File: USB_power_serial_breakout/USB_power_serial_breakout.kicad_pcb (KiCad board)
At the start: 2 copper layers, 45.7 x 26.7 mm, 18 parts, among them J1 Mount2, J2 Mount2, J3 USB_B, J4 UART, U1 FT230XS

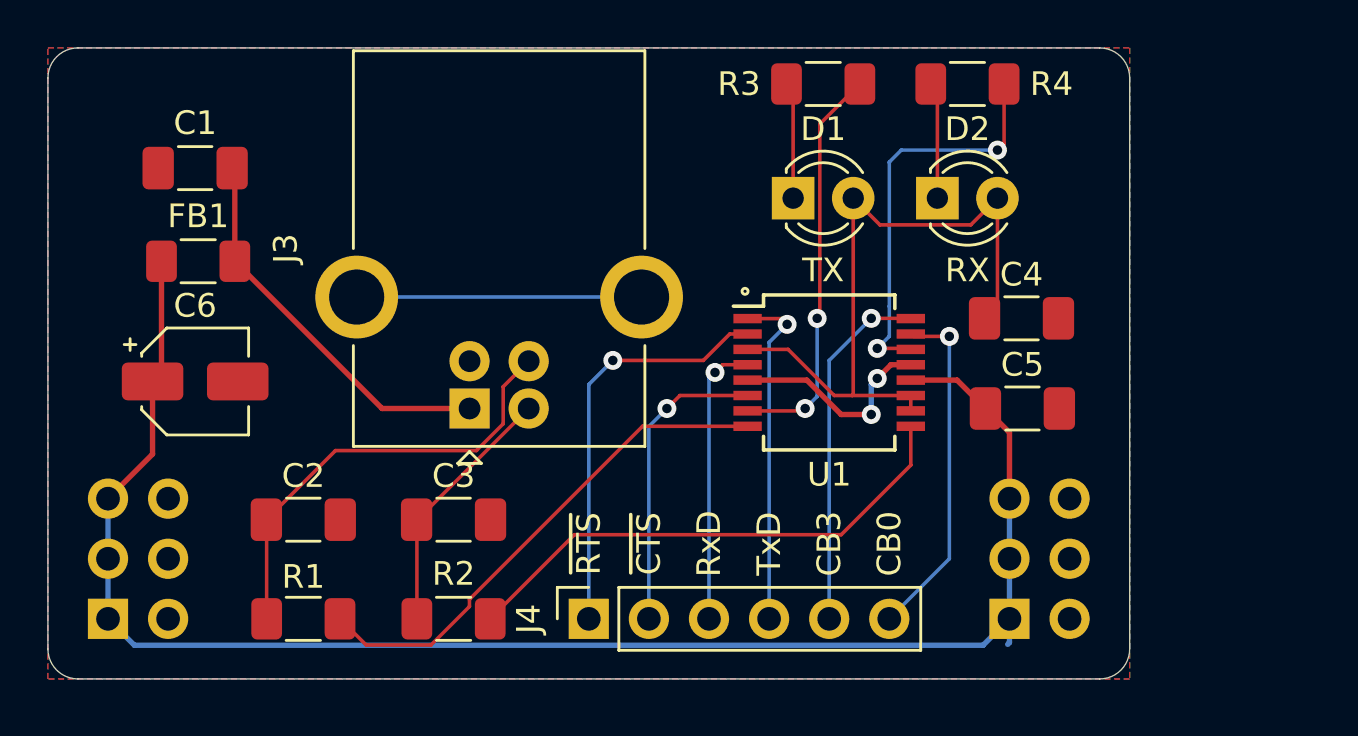
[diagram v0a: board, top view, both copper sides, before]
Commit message: Updated the USB breakout board
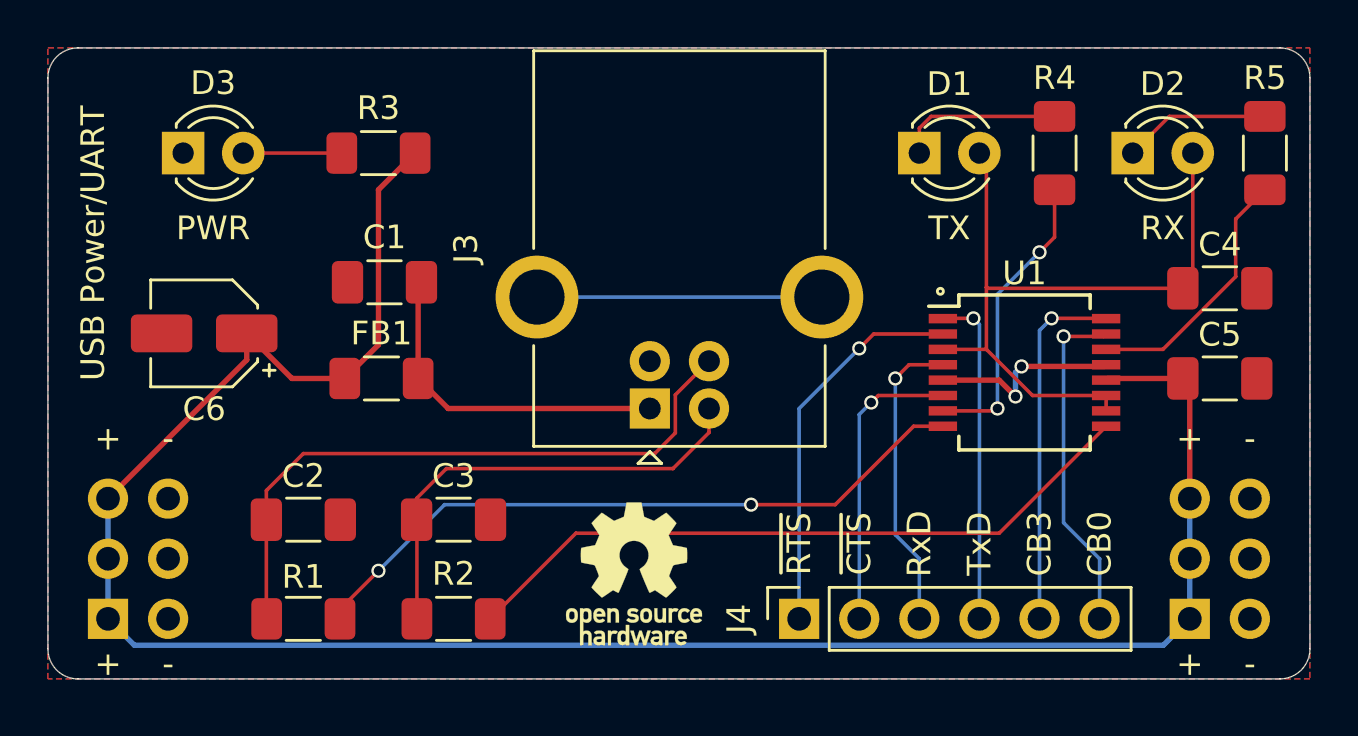
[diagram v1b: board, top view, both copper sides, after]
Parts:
- added D3: PWR, LED_THT:LED_D3.0mm, F.Cu at (196.2, 66.7)
- added QR*****: https://tinyurl.com/ghdbks, kicad_simple:kicad-simple, B.Cu at (200.0, 73.7)
- added R4: 470, Resistor_SMD:R_1206_3216Metric_Pad1.30x1.75mm_HandSolder, F.Cu at (233.0, 66.7)
- added REF**: KiCad-Logo2_5mm_SilkScreen, Symbol:KiCad-Logo2_5mm_SilkScreen, B.Cu at (234.3, 73.7)
- added REF**: OSHW-Logo_5.7x6mm_SilkScreen, Symbol:OSHW-Logo_5.7x6mm_SilkScreen, F.Cu at (215.3, 84.5)
- moved R3 19.0 mm to (204.5, 66.7), turned to 180 degrees
- moved R5 12.9 mm to (241.9, 66.7), turned to 270 degrees
- moved C1 9.34 mm to (204.7, 72.1)
- moved FB1 9.20 mm to (204.6, 76.2)
- moved J4 8.89 mm to (222.2, 86.4)
- moved C4 8.48 mm to (240.0, 72.4)
- moved D2 8.47 mm to (236.3, 66.7)
- moved C5 8.44 mm to (240.0, 76.2)
- moved U1 8.25 mm to (231.8, 75.9)
- moved J2 7.62 mm to (238.8, 86.4)
- moved J3 7.62 mm to (215.9, 77.5)
- moved D1 5.66 mm to (227.3, 66.7)
- moved C6 2.07 mm to (197.1, 74.3), turned to 180 degrees
- renumbered R4 to R5
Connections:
- net Net-(C1-Pad1) renamed /vbus
- R3 pad 1: Net-(D1-Pad1) -> VCC
- R3 pad 2: ~TXLED -> Net-(D3-Pad2)
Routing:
- net VCC: track 69.1 -> 90.4 mm
- net Net-(C3-Pad1): track 10.9 -> 19.6 mm
- net Net-(C2-Pad1): track 19.0 -> 27.3 mm
- net USBD+: track 21.7 -> 29.1 mm, vias 0 -> 2
- net USBD-: track 22.1 -> 29.4 mm
- net ~RXLED: track 17.2 -> 10.9 mm, vias 2 -> 0
- net ~TXLED: track 17.1 -> 12.6 mm
- net Net-(D3-Pad2): track 0.00 -> 4.16 mm
- net /vbus: track 16.5 -> 14.4 mm
- net Net-(D1-Pad1): track 4.94 -> 6.97 mm
- net Net-(C4-Pad1): track 29.1 -> 31.0 mm
- net Net-(D2-Pad1): track 4.94 -> 6.23 mm
- net ~RTS: track 17.5 -> 16.3 mm
- net RxD: track 12.0 -> 12.8 mm
- net GND: track 9.12 -> 8.34 mm
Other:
- board size 45.7 x 26.7 mm -> 53.3 x 26.7 mm
- net class Default: via_dia 0.8 -> 0.6
- net class POWER: via_dia 0.8 -> 0.6
- board text added: "+"
- board text added: "-"
- board text added: "Designed by Dawid Buchwald"
- board text added: "PWR"
- board text added: "USB Power/UART"
- board text added: "Version 1"
